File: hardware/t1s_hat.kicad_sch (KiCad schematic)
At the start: 38 parts, among them CN1 T1S BUS P N N P, J1 2x20 socket (riser stack), U1 LAN8651, Y1 25.000MHz CL12

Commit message: Review follow-ups: GEOMETRY split, BOM/doc consistency, CMC void check, DRC clean, UDP sink
- mechanical/GEOMETRY.md now describes this board only (66.22 x 49.19, no
  notch, 4 holes); the old adapter's outline/notch/6 holes move to
  legacy_adapter_geometry.md
- L1 documented as the 200 uH ACT1210L-201 actually fitted (prototype
  alternative, EMC validation pending); R1/R2 documented as 0.75 W
  substitute for AN1718's 1 W; C4 marked PROTOTYPE_X7R in ORDERING.md
- clock section names the load caps C15/C16 (C1/C2 are the bus caps);
  status LEDs marked as firmware mapping pending
- CMC void forbids tracks on In1/In2/B.Cu; the verifier fails on any
  track or via there, and on F.Cu on anything but L1's nets and the
  known VDDA dogleg (queued for Rev C with test pads and a film CCOMP land)
- NPTH_2.75mm footprint saved to the project library: DRC 0/0/0
- firmware: UDP discard sink on port 9 with a 'sink' command, so blast's
  delivered rate is measured on the far node

Copper, drills and Gerbers are unchanged from Rev B.
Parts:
- R1, R2: value 49R9 1% 1W (DNP) -> 49R9 1% (DNP)
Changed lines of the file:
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@@
       (effects (font (size 1.27 1.27)) (justify left))
     )
-    (property "Value" "49R9 1% 1W (DNP)" (at 327.32 100.93 0)
+    (property "Value" "49R9 1% (DNP)" (at 327.32 100.93 0)
       (effects (font (size 1.27 1.27)) (justify left))
     )
@@
       (effects (font (size 1.27 1.27)) hide)
     )
-    (property "Description" "Bus termination, P leg. 49R9 1% 1W for an END node, 1K5 1% for a DROP node. Shipped unstuffed - see README." (at 325.12 100.33 0)
+    (property "Description" "Bus termination, P leg. 49R9 1% for an END node (AN1718: 1 W; the orderable part is 0.75 W, see ORDERING.md), 1K5 1% for a DROP node. Shipped unstuffed - see README." (at 325.12 100.33 0)
       (effects (font (size 1.27 1.27)) hide)
     )
@@
       (effects (font (size 1.27 1.27)) (justify left))
     )
-    (property "Value" "49R9 1% 1W (DNP)" (at 327.32 139.03 0)
+    (property "Value" "49R9 1% (DNP)" (at 327.32 139.03 0)
       (effects (font (size 1.27 1.27)) (justify left))
     )
@@
       (effects (font (size 1.27 1.27)) hide)
     )
-    (property "Description" "Bus termination, N leg. 49R9 1% 1W for an END node, 1K5 1% for a DROP node. Shipped unstuffed - see README." (at 325.12 138.43 0)
+    (property "Description" "Bus termination, N leg. 49R9 1% for an END node (AN1718: 1 W; the orderable part is 0.75 W, see ORDERING.md), 1K5 1% for a DROP node. Shipped unstuffed - see README." (at 325.12 138.43 0)
       (effects (font (size 1.27 1.27)) hide)
     )

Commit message: JLC CPL in JLC's footprint frame: fix L1 rotation and CN1 origin; D2 restocked
check_jlc_cpl.py places the EasyEDA footprint of every LCSC part exactly as
the CPL says and checks each pad lands on ours. Against the plain KiCad
export it found two parts JLC would have placed wrong:
- L1: EasyEDA's ACT1210 is drawn 90 deg from ours; CPL 90 -> 0
- CN1: EasyEDA's origin is the body centre, KiCad's pin 1; CPL now
  gives the pad centroid (5.715 mm)
Now 0 parts off in all three variants. LEDs are compared by K/A, not
pad number.

D2: C89811 fell to 20 in stock; now KENTO KT-0603Y (C2287), cathode on
the same side. Stock re-checked 2026-09-30. Board unchanged.
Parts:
- D2: LCSC C89811 -> C2287
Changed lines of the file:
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@@
       (effects (font (size 1.27 1.27)) hide)
     )
-    (property "LCSC" "C89811" (at 304.80 214.63 0)
+    (property "LCSC" "C2287" (at 304.80 214.63 0)
       (effects (font (size 1.27 1.27)) hide)
     )

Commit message: Rev C: drop the LEDs the LAN8651 cannot drive, route VDDA clear of the choke, status on the Elite LED
- LAN8651 PADCTRL A0SEL/A1SEL are event capture/generator only - no LED
  function - so D1/D2/R8/R9 go (two extended parts fewer) and DIOA0/1 are
  grounded with DIOA2/3/4
- VDDA leaves pin 29 by two vias under the top lanes instead of running
  0.25 mm inside L1's outline; the CMC-void check needs no exception now
- firmware: Elite LED (IO38) shows PLCA state from PLCA_STS (solid / fast
  blink / slow blink)
- docs: Rev C changes and what was deliberately not done (no DIP/term
  switch, no film CCOMP - none exists in SMD), measured numbers from a
  LAN8651 HAT on this firmware, bring-up order; DRC 0/0/0, CPL check 0 off
Rev B stays at tag rev-b.
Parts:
- removed D1: GRN, LED_SMD:LED_0603_1608Metric, symbol Device:LED
- removed D2: YEL, LED_SMD:LED_0603_1608Metric, symbol Device:LED
- removed R8, R9: 1k, Resistor_SMD:R_0603_1608Metric, symbol Device:R
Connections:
- net LED0_K is gone; now on net GND: U1.18 (DIOA0)
- net LED1_K is gone; now on net GND: U1.19 (DIOA1)
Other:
- note added: "DIOA0..4 and DIOB0/DIOB1 to ground: the LAN8651 has no LED function. Status: the Elite's own LED (IO38)."
- note removed: "STATUS LEDs on DIOA0/DIOA1 (VDDP domain, 1k to 3V3; the DIO sinks). DIOA2/3/4 and DIOB0/DIOB1 to ground."

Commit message: Rev C review fixes: decoupling, RBIAS and crystal at their pins, EP paste clear of vias
Pre-fabrication review of the Rev C layout. Still Rev C; not ordered.

- CCOMP: C5 1.4 mm and C4 2.9 mm from pin 21 (were 2.3 / 6.1 mm), trace
  0.30/0.40 mm and 3.0 mm long (was 0.15 mm, 10.1 mm), own ground vias.
  DIOA0..4 tie inward to the exposed pad to free U1's right edge.
- U1 exposed-pad paste: project-local copy of the TQFN-32 footprint with the
  paste split into 12 windows, each >= 0.15 mm off every thermal via land
  (51 % coverage); land, mask and vias unchanged. Asserted by the verifier.
- VDDAU: C14/C13 2.1/2.6 mm from pin 25 (were 15.4/15.8 mm).
- VDDA: C12 5.0 mm of copper from pin 29 (was 7.1), B.Cu hop now to the
  top-left corner, still clear of the choke void.
- RBIAS: R7 on end beside pin 26, 1.8 mm trace (was 13.3 mm); RBIAS runs
  within 0.6 mm of XTI for 1.4 mm instead of ~10 mm.
- Crystal: XTI 15.7 -> 10.0 mm, XTO 8.3 -> 8.5 mm, load caps at the pads.
- Bus spacing: custom DRC rule BUS_P/BUS_N >= 0.45 mm to any other net
  (t1s_hat.kicad_dru); lanes and MOV stubs adjusted to pass. Net classes
  now really reach the board (0.2 mm, board net names) and the comment that
  claimed otherwise is corrected.
- Silkscreen at J1: "PIN 1 = USB-C END", "TURNED 180 = GND ON 5V".
- erc.rpt regenerated (was Rev B); ELECTRICAL.md: DS60001734F 8.6 gives the
  oscillator gm (18.2 mS nominal, ~16x margin).

DRC 0/0/0 after fill, ERC 0 errors, mechanical error 0, JLC CPL check 0 off
for end/drop/base. Gerbers, drill, BOM/CPL, previews and 3D model rebuilt.
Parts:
- U1: footprint Package_DFN_QFN:TQFN-32-1EP_5x5mm_P0.5mm_EP3.4x3.4mm_ThermalVias -> t1s_hat:TQFN-32-1EP_5x5mm_P0.5mm_EP3.4x3.4mm_ThermalVias_SplitPaste
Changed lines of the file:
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@@
       (effects (font (size 1.27 1.27)) (justify left))
     )
-    (property "Footprint" "Package_DFN_QFN:TQFN-32-1EP_5x5mm_P0.5mm_EP3.4x3.4mm_ThermalVias" (at 190.50 129.54 0)
+    (property "Footprint" "t1s_hat:TQFN-32-1EP_5x5mm_P0.5mm_EP3.4x3.4mm_ThermalVias_SplitPaste" (at 190.50 129.54 0)
       (effects (font (size 1.27 1.27)) hide)
     )

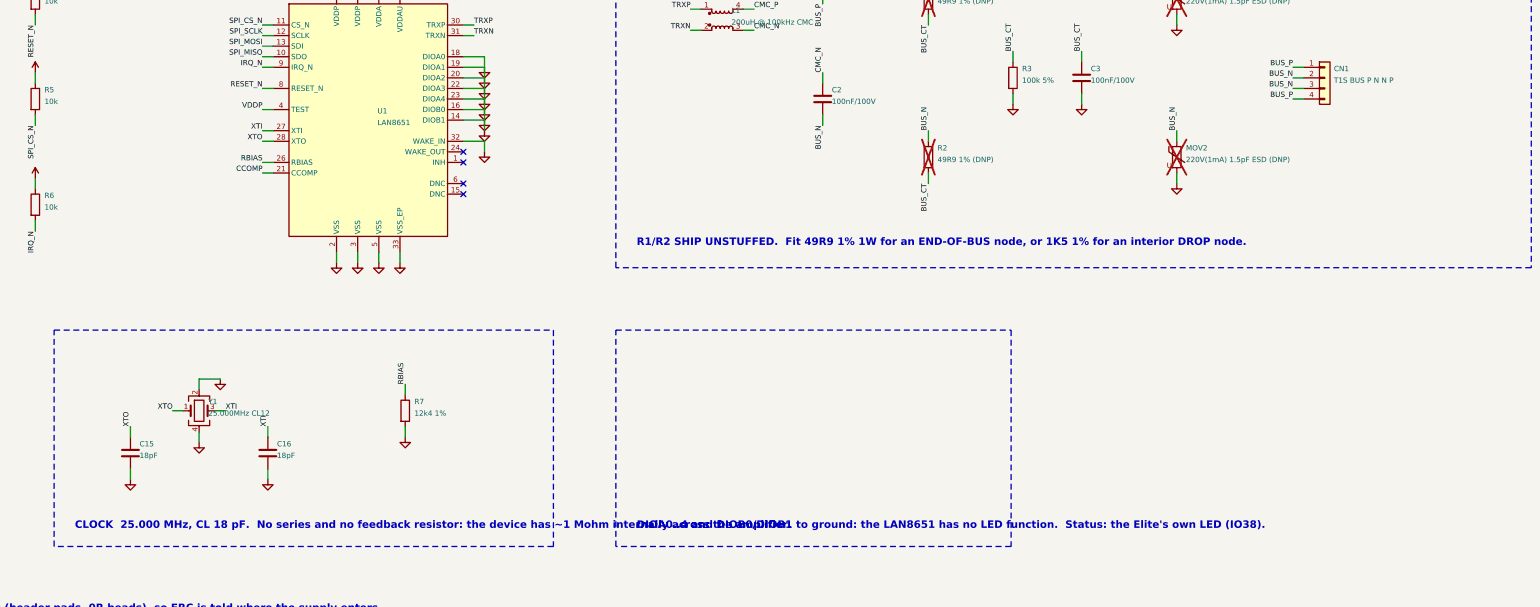
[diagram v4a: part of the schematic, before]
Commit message: Consistency pass from an audit: docs, schematic notes, one silkscreen line
Board: copper, pads and zones unchanged (347 items compared); the termination silkscreen line
reads '49R9 1%' (the fitted part is 0.75 W, the old line said 1 W). Schematic: title rev C,
clock note CL 12 pF, R1/R2 note >=0.5 W; R3 value 100k 1% (C149504 is 0805W8F1003T5E, F = 1%).
Docs: 6 extended parts with end/drop (5 unfitted), 15 BOM lines, 34 parts, Rev B never
ordered, firmware status = runs on hardware, stale LED/riser/580 KB/partition claims fixed,
min clearance 0.20 and the MOV rule described as written, console list complete (tx, wifi,
ota, zenoh), relative pins.h link, no local paths. DRC 0/0/0, ERC 0 errors, CPL 0 off (x3).
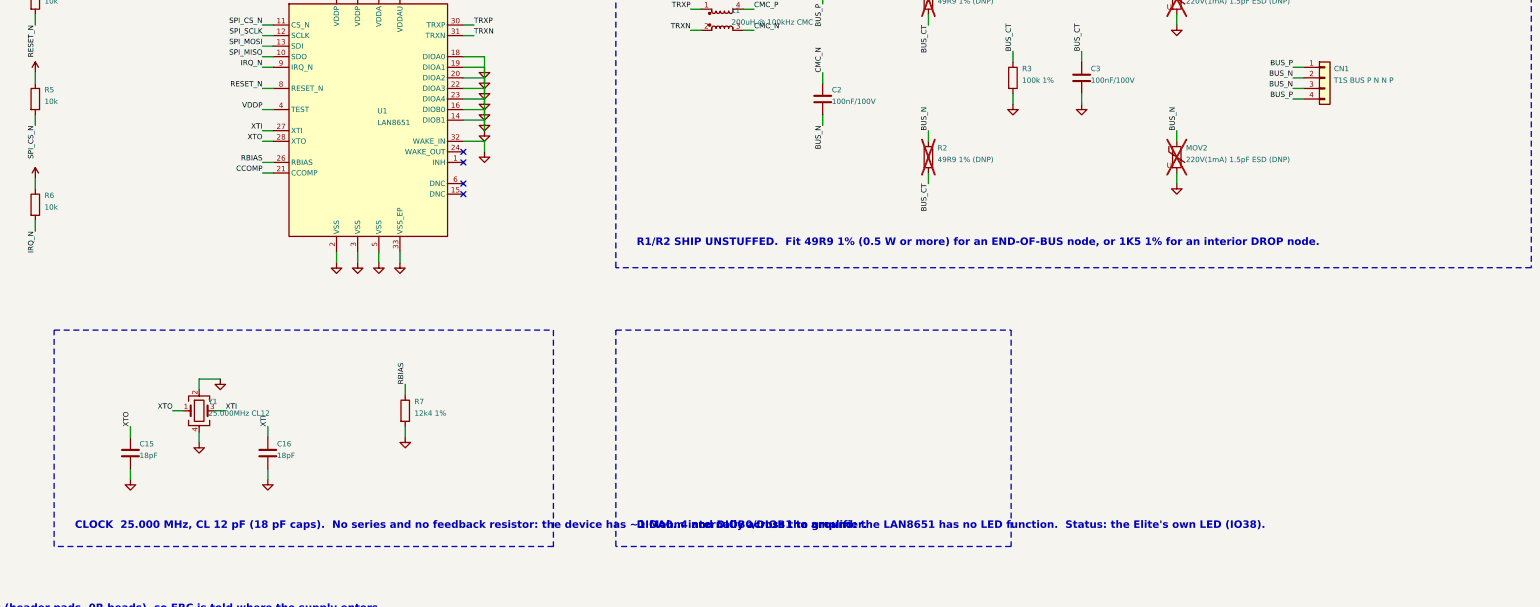
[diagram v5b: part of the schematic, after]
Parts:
- R3: value 100k 5% -> 100k 1%
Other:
- note added: "CLOCK 25.000 MHz, CL 12 pF (18 pF caps). No series and no feedback resistor: the device has ~1 Mohm internally across the amplifier."
- note added: "R1/R2 SHIP UNSTUFFED. Fit 49R9 1% (0.5 W or more) for an END-OF-BUS node, or 1K5 1% for an interior DROP node."
- note removed: "CLOCK 25.000 MHz, CL 18 pF. No series and no feedback resistor: the device has ~1 Mohm internally across the amplifier."
- note removed: "R1/R2 SHIP UNSTUFFED. Fit 49R9 1% 1W for an END-OF-BUS node, or 1K5 1% for an interior DROP node."
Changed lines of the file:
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@@
     (title "T1S HAT - LAN8651 10BASE-T1S")
     (date "")
-    (rev "A")
+    (rev "C")
     (company "")
     (comment 1 "Generated by make_t1s_hat.py from ELECTRICAL.md")
@@
       (effects (font (size 1.27 1.27)) (justify left))
     )
-    (property "Value" "100k 5%" (at 347.64 119.98 0)
+    (property "Value" "100k 1%" (at 347.64 119.98 0)
       (effects (font (size 1.27 1.27)) (justify left))
     )
@@
     (effects (font (size 1.80 1.80) bold) (justify left bottom))
   )
-  (text "R1/R2 SHIP UNSTUFFED.  Fit 49R9 1% 1W for an END-OF-BUS node, or 1K5 1% for an interior DROP node." (at 255.00 160.00 0)
+  (text "R1/R2 SHIP UNSTUFFED.  Fit 49R9 1% (0.5 W or more) for an END-OF-BUS node, or 1K5 1% for an interior DROP node." (at 255.00 160.00 0)
     (effects (font (size 1.80 1.80) bold) (justify left bottom))
   )
-  (text "CLOCK  25.000 MHz, CL 18 pF.  No series and no feedback resistor: the device has ~1 Mohm internally across the amplifier." (at 120.00 228.00 0)
+  (text "CLOCK  25.000 MHz, CL 12 pF (18 pF caps).  No series and no feedback resistor: the device has ~1 Mohm internally across the amplifier." (at 120.00 228.00 0)
     (effects (font (size 1.80 1.80) bold) (justify left bottom))
   )

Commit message: Rev D: push-in spring terminal for the bus (Kefa KF141R-2.54-4P, LCSC C475126) instead of the pluggable Phoenix MC header; pads in two rows, P bridge between them, front/back pads tied on B.Cu; DRC 0, ERC unchanged, JLC CPL exact
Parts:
- CN1: footprint Connector_Phoenix_MC:PhoenixContact_MC_1,5_4-G-3.81_1x04_P3.81mm_Horizontal -> t1s_hat:TerminalBlock_Kefa_KF141R-2.54-4P; LCSC C480536 -> C475126
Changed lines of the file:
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@@
     (title "T1S HAT - LAN8651 10BASE-T1S")
     (date "")
-    (rev "C")
+    (rev "D")
     (company "")
     (comment 1 "Generated by make_t1s_hat.py from ELECTRICAL.md")
@@
       (effects (font (size 1.27 1.27)) (justify left))
     )
-    (property "Footprint" "Connector_Phoenix_MC:PhoenixContact_MC_1,5_4-G-3.81_1x04_P3.81mm_Horizontal" (at 420.37 119.38 0)
+    (property "Footprint" "t1s_hat:TerminalBlock_Kefa_KF141R-2.54-4P" (at 420.37 119.38 0)
       (effects (font (size 1.27 1.27)) hide)
     )
@@
       (effects (font (size 1.27 1.27)) hide)
     )
-    (property "Description" "MDI connector, 4-pin 3.81 mm pluggable terminal block. Pins 1..4 = P N N P; the two P and the two N are shorted on board so the node taps a daisy chain." (at 420.37 119.38 0)
-      (effects (font (size 1.27 1.27)) hide)
-    )
-    (property "LCSC" "C480536" (at 420.37 119.38 0)
-      (effects (font (size 1.27 1.27)) hide)
-    )
+    (property "Description" "MDI connector, 4-pin 2.54 mm push-in spring terminal (lever). Pins 1..4 = P N N P; the two P and the two N are shorted on board so the node taps a daisy chain." (at 420.37 119.38 0)
+      (effects (font (size 1.27 1.27)) hide)
+    )
+    (property "LCSC" "C475126" (at 420.37 119.38 0)
+      (effects (font (size 1.27 1.27)) hide)
+    )

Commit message: Rev D: CS off the BOOT strap (header 27 = IO8), DIOA4 1PPS to TP1 and header 13 (IO40)
Review bugs from Rev C. PPS leaves U1 pin 23 through a via and runs on B.Cu;
R5's +3V3 via moved 1 mm left for the CS lane. DRC 0, ERC 0 errors (6 warnings,
DIOA4 no longer grounded), JLC CPL exact.

Firmware: CS found at boot by reading DEVID on IO0 then IO8; ptp pps on drives
the dedicated 1PPS (PADCTRL A4SEL, PPSCTL) and counts edges on IO40. The EG0
path had its registers one too high (0x222.. vs DS60001734F 0x221..); fixed,
now ptp pps eg0 force.
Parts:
- added TP1: PPS, TestPoint:TestPoint_Pad_D1.5mm, symbol Connector:TestPoint
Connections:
- net GND: no longer U1.23 (DIOA4)
- net SPI_CS_N: now also J1.27 (ID_SD); no longer J1.24 (GPIO8/CE0)
- net PPS: now reaches J1.13 (GPIO27)
- net PPS: now also U1.23 (DIOA4), TP1.1
- no-connect marks 28 -> 27
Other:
- note added: "DIOA0..3 and DIOB0/DIOB1 to ground (no LED function; status on the Elite's LED, IO38). DIOA4 = 1PPS to TP1 and IO40."
- note removed: "DIOA0..4 and DIOB0/DIOB1 to ground: the LAN8651 has no LED function. Status: the Elite's own LED (IO38)."
